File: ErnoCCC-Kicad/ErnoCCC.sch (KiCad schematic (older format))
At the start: 88 parts, among them J1 6VAC, J2 ICSP, J3 FTDI, J4 Erno Controller, J5 SWITCH, J6 LED OUT, J7 Conn_01x07, Q1 BC847, Q2 BC847, Q3 BC847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

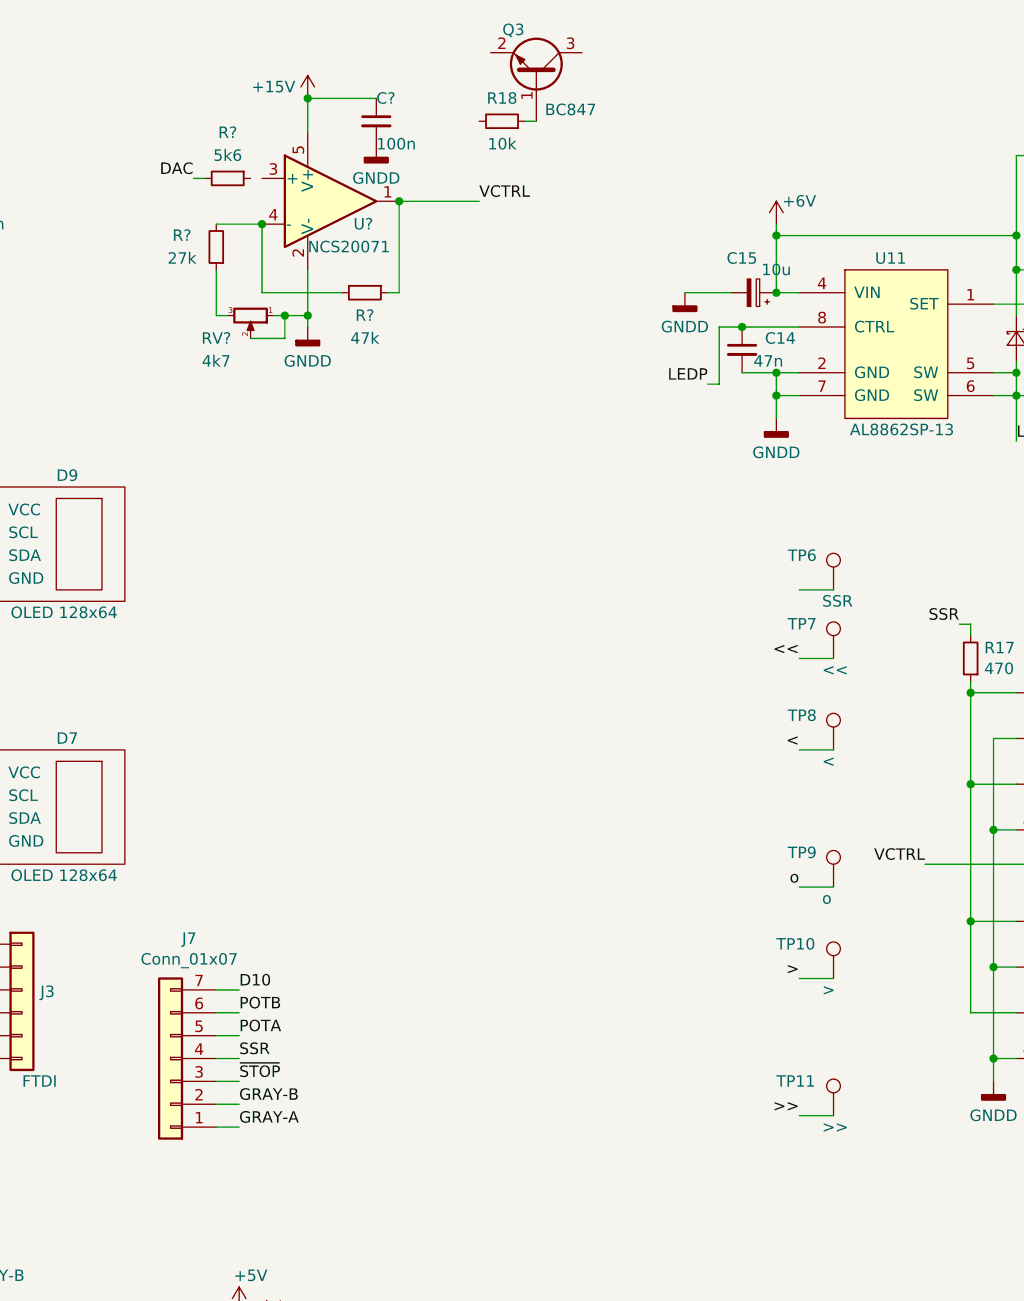
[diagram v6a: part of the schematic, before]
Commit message: Preparing for the big refactoring (old footprints still there)
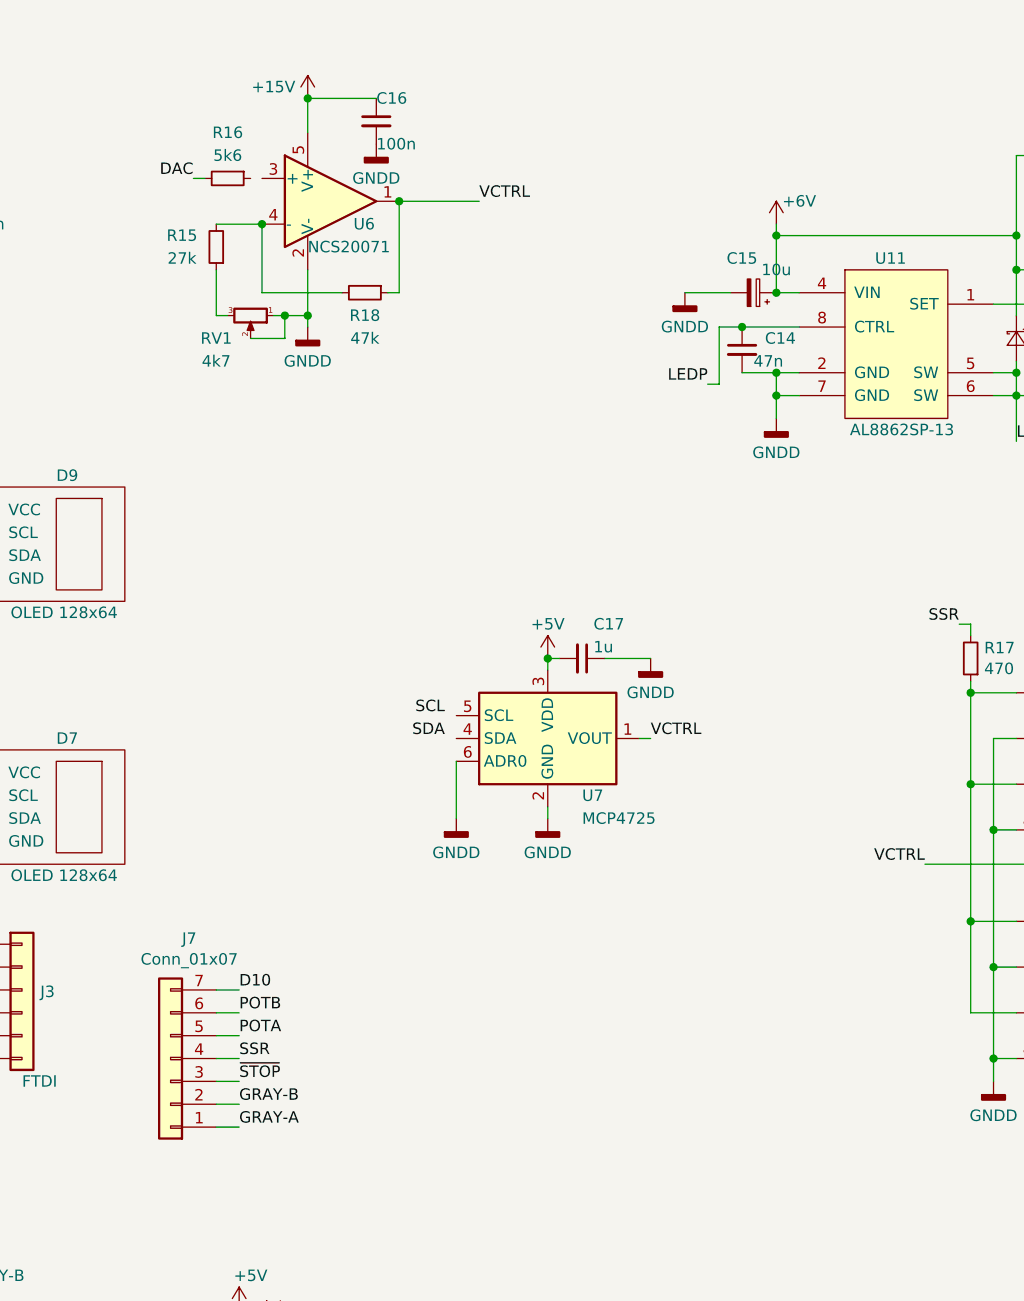
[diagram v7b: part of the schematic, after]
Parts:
- removed Q3: BC847, Package_TO_SOT_SMD:SOT-23, symbol Transistor_BJT:BC847
- removed R18: 10k, Resistor_SMD:R_0805_2012Metric, symbol Device:R_Small
- removed TP10: >, TestPoint:TestPoint_THTPad_D1.5mm_Drill0.7mm, symbol Connector:TestPoint
- removed TP11: >>, TestPoint:TestPoint_THTPad_D1.5mm_Drill0.7mm, symbol Connector:TestPoint
- removed TP6: SSR, TestPoint:TestPoint_THTPad_D1.5mm_Drill0.7mm, symbol Connector:TestPoint
- removed TP7: <<, TestPoint:TestPoint_THTPad_D1.5mm_Drill0.7mm, symbol Connector:TestPoint
- removed TP8: <, TestPoint:TestPoint_THTPad_D1.5mm_Drill0.7mm, symbol Connector:TestPoint
- removed TP9: o, TestPoint:TestPoint_THTPad_D1.5mm_Drill0.7mm, symbol Connector:TestPoint
- added C17: 1u, Capacitor_SMD:C_0805_2012Metric, symbol Device:C_Small
- added U7: MCP4725, Package_TO_SOT_SMD:SOT-23-6, symbol Analog_DAC:MCP4725
- gave numbers to parts that had none: 6
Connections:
- net +5V: now also C17.2, U7.3 (VDD)
- net GND: now also C17.1, U7.2 (GND), U7.6 (ADR0)
- net VCTRL: now also U7.1 (VOUT)
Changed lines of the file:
@@
 Text Notes 10400 3350 0    50   ~ 0
 Blue (Pot)
-Text Label 8150 3150 2    50   ~ 0
-<<
-Text Label 8150 3550 2    50   ~ 0
-<
-Text Label 8150 4150 2    50   ~ 0
-o
-Text Label 8150 4550 2    50   ~ 0
->
-Text Label 8150 5150 2    50   ~ 0
->>
 Wire Wire Line
 	8900 3250 8900 3300
@@
 Wire Wire Line
 	2000 4800 2150 4800
-$Comp
-L Connector:TestPoint TP8
-U 1 1 5E56BF42
-P 8300 3550
-F 0 "TP8" H 8100 3700 50  0000 L CNN
-F 1 "<" H 8250 3500 50  0000 L CNN
-F 2 "TestPoint:TestPoint_THTPad_D1.5mm_Drill0.7mm" H 8500 3550 50  0001 C CNN
-F 3 "~" H 8500 3550 50  0001 C CNN
-	1    8300 3550
-	1    0    0    -1
-$EndComp
-$Comp
-L Connector:TestPoint TP7
-U 1 1 5E570475
-P 8300 3150
-F 0 "TP7" H 8100 3300 50  0000 L CNN
-F 1 "<<" H 8250 3100 50  0000 L CNN
-F 2 "TestPoint:TestPoint_THTPad_D1.5mm_Drill0.7mm" H 8500 3150 50  0001 C CNN
-F 3 "~" H 8500 3150 50  0001 C CNN
-	1    8300 3150
-	1    0    0    -1
-$EndComp
-$Comp
-L Connector:TestPoint TP9
-U 1 1 5E570F18
-P 8300 4150
-F 0 "TP9" H 8100 4300 50  0000 L CNN
-F 1 "o" H 8250 4100 50  0000 L CNN
-F 2 "TestPoint:TestPoint_THTPad_D1.5mm_Drill0.7mm" H 8500 4150 50  0001 C CNN
-F 3 "~" H 8500 4150 50  0001 C CNN
-	1    8300 4150
-	1    0    0    -1
-$EndComp
-$Comp
-L Connector:TestPoint TP10
-U 1 1 5E5713A7
-P 8300 4550
-F 0 "TP10" H 8050 4700 50  0000 L CNN
-F 1 ">" H 8250 4500 50  0000 L CNN
-F 2 "TestPoint:TestPoint_THTPad_D1.5mm_Drill0.7mm" H 8500 4550 50  0001 C CNN
-F 3 "~" H 8500 4550 50  0001 C CNN
-	1    8300 4550
-	1    0    0    -1
-$EndComp
-$Comp
-L Connector:TestPoint TP11
-U 1 1 5E571752
-P 8300 5150
-F 0 "TP11" H 8050 5300 50  0000 L CNN
-F 1 ">>" H 8250 5100 50  0000 L CNN
-F 2 "TestPoint:TestPoint_THTPad_D1.5mm_Drill0.7mm" H 8500 5150 50  0001 C CNN
-F 3 "~" H 8500 5150 50  0001 C CNN
-	1    8300 5150
-	1    0    0    -1
-$EndComp
-$Comp
-L Connector:TestPoint TP6
-U 1 1 5E571A52
-P 8300 2850
-F 0 "TP6" H 8100 3000 50  0000 L CNN
-F 1 "SSR" H 8250 2800 50  0000 L CNN
-F 2 "TestPoint:TestPoint_THTPad_D1.5mm_Drill0.7mm" H 8500 2850 50  0001 C CNN
-F 3 "~" H 8500 2850 50  0001 C CNN
-	1    8300 2850
-	1    0    0    -1
-$EndComp
-Wire Wire Line
-	8150 2850 8300 2850
-Wire Wire Line
-	8150 3150 8300 3150
-Wire Wire Line
-	8150 3550 8300 3550
-Wire Wire Line
-	8150 4150 8300 4150
-Wire Wire Line
-	8150 4550 8300 4550
-Wire Wire Line
-	8150 5150 8300 5150
 $Comp
 L 74xx:74HC14 U4
@@
 	4400 3850 4450 3850
 $Comp
-L ErnoCCC-rescue:NCS20071-Amplifier_Operational U?
+L ErnoCCC-rescue:NCS20071-Amplifier_Operational U6
 U 1 1 5E204FD7
 P 6100 1150
-F 0 "U?" H 6200 1050 50  0000 L CNN
+F 0 "U6" H 6200 1050 50  0000 L CNN
 F 1 "NCS20071" H 6000 950 50  0000 L CNN
 F 2 "Package_TO_SOT_SMD:TSOT-23-5" H 6100 1150 50  0001 C CNN
@@
 $EndComp
 $Comp
-L Device:R_Small R?
+L Device:R_Small R18
 U 1 1 5E2064E3
 P 6250 1550
-F 0 "R?" V 6350 1550 50  0000 C CNN
+F 0 "R18" V 6350 1550 50  0000 C CNN
 F 1 "47k" V 6450 1550 50  0000 C CNN
 F 2 "Resistor_SMD:R_1210_3225Metric" H 6250 1550 50  0001 C CNN
@@
 $EndComp
 $Comp
-L Device:R_Small R?
+L Device:R_Small R15
 U 1 1 5E206C0A
 P 5600 1350
-F 0 "R?" H 5750 1300 50  0000 C CNN
+F 0 "R15" H 5750 1300 50  0000 C CNN
 F 1 "27k" H 5750 1400 50  0000 C CNN
 F 2 "Resistor_SMD:R_1210_3225Metric" H 5600 1350 50  0001 C CNN
@@
 $EndComp
 $Comp
-L Device:R_POT_Small RV?
+L Device:R_POT_Small RV1
 U 1 1 5E208E10
 P 5750 1650
-F 0 "RV?" V 5850 1500 50  0000 C CNN
+F 0 "RV1" V 5850 1500 50  0000 C CNN
 F 1 "4k7" V 5950 1500 50  0000 C CNN
 F 2 "Potentiometer_THT:Potentiometer_Bourns_3296W_Vertical" H 5750 1650 50  0001 C CNN
@@
 $EndComp
 $Comp
-L power:GNDD #PWR?
+L power:GNDD #PWR020
 U 1 1 5E20C34F
 P 6000 1700
-F 0 "#PWR?" H 6000 1450 50  0001 C CNN
+F 0 "#PWR020" H 6000 1450 50  0001 C CNN
 F 1 "GNDD" H 6000 1550 50  0000 C CNN
 F 2 "" H 6000 1700 50  0001 C CNN
@@
 GND
 $Comp
-L power:+15V #PWR?
+L power:+15V #PWR032
 U 1 1 5E443EB7
 P 10050 3200
-F 0 "#PWR?" H 10050 3050 50  0001 C CNN
+F 0 "#PWR032" H 10050 3050 50  0001 C CNN
 F 1 "+15V" H 10065 3373 50  0000 C CNN
 F 2 "" H 10050 3200 50  0001 C CNN
@@
 Green (Pot)
 Wire Wire Line
-	6950 800  7000 800
-$Comp
-L Device:R_Small R18
-U 1 1 5E919A23
-P 6850 800
-F 0 "R18" V 6950 800 50  0000 C CNN
-F 1 "10k" V 6750 800 50  0000 C CNN
-F 2 "Resistor_SMD:R_0805_2012Metric" H 6850 800 50  0001 C CNN
-F 3 "~" H 6850 800 50  0001 C CNN
-	1    6850 800
-	0    1    -1   0
-$EndComp
-$Comp
-L Transistor_BJT:BC847 Q3
-U 1 1 5E916B0B
-P 7000 600
-F 0 "Q3" V 7200 500 50  0000 C CNN
-F 1 "BC847" V 6850 750 50  0000 C CNN
-F 2 "Package_TO_SOT_SMD:SOT-23" H 7200 525 50  0001 L CIN
-F 3 "https://www.mouser.de/datasheet/2/308/BC846ALT1-D-1293035.pdf" H 7000 600 50  0001 L CNN
-	1    7000 600
-	0    1    -1   0
-$EndComp
-Wire Wire Line
 	9950 4300 9950 3600
 Wire Wire Line
@@
 VCTRL
 $Comp
-L power:GNDD #PWR?
+L power:GNDD #PWR033
 U 1 1 5E7172A8
 P 10150 3900
-F 0 "#PWR?" H 10150 3650 50  0001 C CNN
+F 0 "#PWR033" H 10150 3650 50  0001 C CNN
 F 1 "GNDD" H 10150 3750 50  0000 C CNN
 F 2 "" H 10150 3900 50  0001 C CNN
@@
 	10150 3200 10050 3200
 $Comp
-L power:+15V #PWR?
+L power:+15V #PWR019
 U 1 1 5E74D1BD
 P 6000 700
-F 0 "#PWR?" H 6000 550 50  0001 C CNN
+F 0 "#PWR019" H 6000 550 50  0001 C CNN
 F 1 "+15V" H 5850 750 50  0000 C CNN
 F 2 "" H 6000 700 50  0001 C CNN
@@
 	6000 700  6000 850
 $Comp
-L Device:C_Small C?
+L Device:C_Small C16
 U 1 1 5E768765
 P 6300 800
-F 0 "C?" H 6300 900 50  0000 L CNN
+F 0 "C16" H 6300 900 50  0000 L CNN
 F 1 "100n" H 6300 700 50  0000 L CNN
 F 2 "Capacitor_SMD:C_0805_2012Metric" H 6300 800 50  0001 C CNN
@@
 Connection ~ 6000 700
 $Comp
-L power:GNDD #PWR?
+L power:GNDD #PWR021
 U 1 1 5E7BC36F
 P 6300 900
-F 0 "#PWR?" H 6300 650 50  0001 C CNN
+F 0 "#PWR021" H 6300 650 50  0001 C CNN
 F 1 "GNDD" H 6300 750 50  0000 C CNN
 F 2 "" H 6300 900 50  0001 C CNN
@@
 $EndComp
 $Comp
-L Device:R_Small R?
+L Device:R_Small R16
 U 1 1 5E7BC9BF
 P 5650 1050
-F 0 "R?" V 5450 1050 50  0000 C CNN
+F 0 "R16" V 5450 1050 50  0000 C CNN
 F 1 "5k6" V 5550 1050 50  0000 C CNN
 F 2 "Resistor_SMD:R_1210_3225Metric" H 5650 1050 50  0001 C CNN
@@
 	9000 4900 9000 5000
 Connection ~ 9000 4900
+$Comp
+L Analog_DAC:MCP4725 U7
+U 1 1 5E234717
+P 7050 3500
+F 0 "U7" H 7200 3250 50  0000 L CNN
+F 1 "MCP4725" H 7200 3150 50  0000 L CNN
+F 2 "Package_TO_SOT_SMD:SOT-23-6" H 7700 3250 50  0001 C CNN
+F 3 "http://www.ti.com/lit/ds/symlink/dac081c081.pdf" H 7050 3500 50  0001 C CNN
+	1    7050 3500
+	1    0    0    -1
+$EndComp
+$Comp
+L power:GNDD #PWR030
+U 1 1 5E23515D
+P 7050 3850
+F 0 "#PWR030" H 7050 3600 50  0001 C CNN
+F 1 "GNDD" H 7050 3700 50  0000 C CNN
+F 2 "" H 7050 3850 50  0001 C CNN
+F 3 "" H 7050 3850 50  0001 C CNN
+	1    7050 3850
+	1    0    0    -1
+$EndComp
+$Comp
+L power:+5V #PWR029
+U 1 1 5E235578
+P 7050 3150
+F 0 "#PWR029" H 7050 3000 50  0001 C CNN
+F 1 "+5V" H 7050 3300 50  0000 C CNN
+F 2 "" H 7050 3150 50  0001 C CNN
+F 3 "" H 7050 3150 50  0001 C CNN
+	1    7050 3150
+	1    0    0    -1
+$EndComp
+Wire Wire Line
+	7050 3150 7050 3200
+Wire Wire Line
+	7050 3800 7050 3850
+Text Label 7500 3500 0    50   ~ 0
+VCTRL
+Wire Wire Line
+	7450 3500 7500 3500
+Text Label 6600 3500 2    50   ~ 0
+SDA
+Text Label 6600 3400 2    50   ~ 0
+SCL
+$Comp
+L Device:C_Small C17
+U 1 1 5E28031F
+P 7200 3150
+F 0 "C17" V 7050 3200 50  0000 L CNN
+F 1 "1u" V 7150 3200 50  0000 L CNN
+F 2 "Capacitor_SMD:C_0805_2012Metric" H 7200 3150 50  0001 C CNN
+F 3 "~" H 7200 3150 50  0001 C CNN
+	1    7200 3150
+	0    1    1    0
+$EndComp
+Wire Wire Line
+	7100 3150 7050 3150
+Connection ~ 7050 3150
+$Comp
+L power:GNDD #PWR031
+U 1 1 5E29A55E
+P 7500 3150
+F 0 "#PWR031" H 7500 2900 50  0001 C CNN
+F 1 "GNDD" H 7500 3000 50  0000 C CNN
+F 2 "" H 7500 3150 50  0001 C CNN
+F 3 "" H 7500 3150 50  0001 C CNN
+	1    7500 3150
+	1    0    0    -1
+$EndComp
+Wire Wire Line
+	7300 3150 7500 3150
+$Comp
+L power:GNDD #PWR028
+U 1 1 5E2B49E3
+P 6650 3850
+F 0 "#PWR028" H 6650 3600 50  0001 C CNN
+F 1 "GNDD" H 6650 3700 50  0000 C CNN
+F 2 "" H 6650 3850 50  0001 C CNN
+F 3 "" H 6650 3850 50  0001 C CNN
+	1    6650 3850
+	1    0    0    -1
+$EndComp
+Wire Wire Line
+	6650 3600 6650 3850
 $EndSCHEMATC

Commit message: Preparing for the big RevB rerouting
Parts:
- removed TP15: D10, TestPoint:TestPoint_THTPad_D1.5mm_Drill0.7mm, symbol Connector:TestPoint
- J7: value Conn_01x07 -> Conn_01x05; footprint Connector_PinHeader_2.54mm:PinHeader_1x07_P2.54mm_Horizontal -> Connector_PinHeader_2.54mm:PinHeader_1x05_P2.54mm_Horizontal; symbol Connector_Generic:Conn_01x07 -> Connector_Generic:Conn_01x05
- R15, R16, R18: footprint Resistor_SMD:R_1210_3225Metric -> Resistor_SMD:R_0805_2012Metric
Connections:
- net POTA is gone; now on net D10: J7.5 (Pin_5)
- net D10: no longer J7.7 (Pin_7)
- net SSR: now also J7.3 (Pin_3); no longer J7.4 (Pin_4)
- net at U6.3 (+): now also R16.1
- removed net POTB: J7.6 (Pin_6)
- net ~STOP~ renamed D9
- net D9: now also J7.4 (Pin_4); no longer J7.3 (Pin_3)
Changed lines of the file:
@@
 Wire Wire Line
 	5900 7000 5950 7000
-Text Label 2150 2500 0    50   ~ 0
-~STOP~
 Wire Wire Line
 	2000 4600 2150 4600
@@
 D10
 $Comp
-L Connector:TestPoint TP15
-U 1 1 5E0E3D08
-P 2400 2600
-F 0 "TP15" V 2350 2800 50  0000 L CNN
-F 1 "D10" V 2350 2550 50  0000 L CNN
-F 2 "TestPoint:TestPoint_THTPad_D1.5mm_Drill0.7mm" H 2600 2600 50  0001 C CNN
-F 3 "~" H 2600 2600 50  0001 C CNN
-	1    2400 2600
-	0    1    1    0
-$EndComp
-Wire Wire Line
-	2000 2600 2400 2600
-$Comp
-L Connector_Generic:Conn_01x07 J7
+L Connector_Generic:Conn_01x05 J7
 U 1 1 5E107107
 P 5400 4900
 F 0 "J7" H 5318 4375 50  0000 C CNN
-F 1 "Conn_01x07" H 5318 4466 50  0000 C CNN
-F 2 "Connector_PinHeader_2.54mm:PinHeader_1x07_P2.54mm_Horizontal" H 5400 4900 50  0001 C CNN
+F 1 "Conn_01x05" H 5318 4466 50  0000 C CNN
+F 2 "Connector_PinHeader_2.54mm:PinHeader_1x05_P2.54mm_Horizontal" H 5400 4900 50  0001 C CNN
 F 3 "~" H 5400 4900 50  0001 C CNN
 	1    5400 4900
 	-1   0    0    1
 $EndComp
-Text Label 5700 4600 0    50   ~ 0
+Text Label 5700 4700 0    50   ~ 0
 D10
-Text Label 5700 5000 0    50   ~ 0
-~STOP~
 Text Label 4500 7200 0    50   ~ 0
 GRAY-A
@@
 Wire Wire Line
 	4500 7000 4500 7200
-Text Label 5700 5200 0    50   ~ 0
+Text Label 5700 5100 0    50   ~ 0
 GRAY-A
-Text Label 5700 5100 0    50   ~ 0
+Text Label 5700 5000 0    50   ~ 0
 GRAY-B
 Text Label 5700 4900 0    50   ~ 0
 SSR
-Text Label 5700 4800 0    50   ~ 0
-POTA
-Text Label 5700 4700 0    50   ~ 0
-POTB
-Wire Wire Line
-	5600 4600 5700 4600
 Wire Wire Line
 	5600 4700 5700 4700
 Wire Wire Line
-	5600 4800 5700 4800
-Wire Wire Line
-	5600 4900 5700 4900
-Wire Wire Line
 	5600 5000 5700 5000
 Wire Wire Line
 	5600 5100 5700 5100
-Wire Wire Line
-	5600 5200 5700 5200
 $Comp
 L Jumper:SolderJumper_3_Bridged12 JP3
@@
 F 0 "R18" V 6350 1550 50  0000 C CNN
 F 1 "47k" V 6450 1550 50  0000 C CNN
-F 2 "Resistor_SMD:R_1210_3225Metric" H 6250 1550 50  0001 C CNN
+F 2 "Resistor_SMD:R_0805_2012Metric" H 6250 1550 50  0001 C CNN
 F 3 "~" H 6250 1550 50  0001 C CNN
 	1    6250 1550
@@
 F 0 "R15" H 5750 1300 50  0000 C CNN
 F 1 "27k" H 5750 1400 50  0000 C CNN
-F 2 "Resistor_SMD:R_1210_3225Metric" H 5600 1350 50  0001 C CNN
+F 2 "Resistor_SMD:R_0805_2012Metric" H 5600 1350 50  0001 C CNN
 F 3 "~" H 5600 1350 50  0001 C CNN
 	1    5600 1350
@@
 F 0 "R16" V 5450 1050 50  0000 C CNN
 F 1 "5k6" V 5550 1050 50  0000 C CNN
-F 2 "Resistor_SMD:R_1210_3225Metric" H 5650 1050 50  0001 C CNN
+F 2 "Resistor_SMD:R_0805_2012Metric" H 5650 1050 50  0001 C CNN
 F 3 "~" H 5650 1050 50  0001 C CNN
 	1    5650 1050
@@
 Wire Wire Line
 	6650 3600 6650 3850
+Wire Wire Line
+	5800 1050 5750 1050
+Text Label 2150 2500 0    50   ~ 0
+D9
+Wire Wire Line
+	2000 2600 2150 2600
+Text Label 5700 4800 0    50   ~ 0
+D9
+Wire Wire Line
+	5600 4800 5700 4800
+Wire Wire Line
+	5600 4900 5700 4900
 $EndSCHEMATC
